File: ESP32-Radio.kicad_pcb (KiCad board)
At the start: 2 copper layers, 69 parts, among them J1 BNC, J11 Conn_01x04_Female, J2 Audio_Jack, J3 Pad, J4 Pad, J6 Audio_Jack, J8 PCB_SMA, T1 6:31, T2 31:6, T3 T50_SPLITTER, T4 T50_SPLITTER, U1 LM358, U10 si5351, U11 LD33V, U2 LM358, U3 LM358, U6 MCP1703A-2502_SOT223, U7 FST3253, U8 FST3253

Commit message: added pa
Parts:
- removed C10, C7, C9: 470nF, Xenir:Capacitor 0805
- removed C15: .1uF, Xenir:Capacitor 0805
- removed C17, C18, C19, C20: 10uF, Xenir:Cap_4x5.4
- removed C28: .1uF, Xenir:Capacitor 1206
- removed J3, J4: Pad, Xenir:Pad
- removed J8: PCB_SMA, Xenir:PCB SMA
- removed R10, R23, R7, R8, R9: 100, Xenir:Resistor 0805
- removed T2: 31:6, Xenir:T37 Transformer
- removed T3, T4: T50_SPLITTER, Xenir:T50 Trifilar
- removed U3: LM358, Xenir:SOIC8
- removed U7: FST3253, Xenir:SO16
- removed VC1, VC2: 40pF, Xenir:trimcap
- added  : MountingHole_3.2mm_M3, MountingHole:MountingHole_3.2mm_M3, F.Cu at (262.4, 96.0)
- added  : MountingHole_3.2mm_M3, MountingHole:MountingHole_3.2mm_M3, F.Cu at (149.8, 96.0)
- added  : MountingHole_3.2mm_M3, MountingHole:MountingHole_3.2mm_M3, F.Cu at (262.4, 160.4)
- added  : MountingHole_3.2mm_M3, MountingHole:MountingHole_3.2mm_M3, F.Cu at (149.8, 160.4)
- added C51: .1uF, Xenir:Capacitor 0805, F.Cu at (206.2, 118.8)
- added C52: .1uF, Xenir:Capacitor 0805, F.Cu at (208.0, 120.6)
- added C53: .1uF, Xenir:Capacitor 0805, F.Cu at (200.7, 96.9)
- added C55: .1uF, Xenir:Capacitor 0805, F.Cu at (222.0, 127.1)
- added C57: .1uF, Xenir:Capacitor 0805, F.Cu at (239.1, 140.0)
- added D1: 1N914, Diode_SMD:D_SOD-323_HandSoldering, F.Cu at (222.5, 122.2)
- added D2: D_Zener, Diode_THT:D_A-405_P10.16mm_Horizontal, F.Cu at (230.2, 142.5)
- added L1: Inductor, Xenir:T37_Inductor, F.Cu at (214.2, 104.9)
- added L2: Inductor, Xenir:T37_Inductor, F.Cu at (234.7, 98.9)
- added L3: 10T T37-6, Xenir:T37_Inductor, F.Cu at (253.7, 133.4)
- added L4: 11T T37-6, Xenir:T37_Inductor, F.Cu at (239.9, 121.7)
- added Q1: 2N3904-SMD, Package_TO_SOT_SMD:SOT-23, F.Cu at (206.5, 125.5)
- added Q2: 2SC5706, Package_TO_SOT_SMD:TO-252-2, F.Cu at (213.1, 115.0)
- added Q3: 2SC5706, Package_TO_SOT_SMD:TO-252-2, F.Cu at (230.0, 119.5)
- added R52: 1k, Xenir:Resistor 0805, F.Cu at (221.5, 122.1)
- added R53: 1k, Xenir:Resistor 0805, F.Cu at (215.9, 128.5)
- added R54: 10k, Xenir:Resistor 0805, F.Cu at (214.4, 118.7)
- added R55: 10, Xenir:Resistor 0805, F.Cu at (217.0, 112.2)
- added R56: 1k, Xenir:Resistor 0805, F.Cu at (205.8, 111.2)
- added R57: 1k, Xenir:Resistor 0805, F.Cu at (220.0, 127.1)
- added R58: 100, Xenir:Resistor 0805, F.Cu at (226.6, 125.2)
- added R59: 1, Resistor_THT:R_Axial_DIN0204_L3.6mm_D1.6mm_P2.54mm_Vertical, F.Cu at (230.2, 133.2)
- added R60: 1, Resistor_THT:R_Axial_DIN0204_L3.6mm_D1.6mm_P2.54mm_Vertical, F.Cu at (230.2, 137.2)
- C1, C2: value 1nF -> .1uF
- C3: value 150pF -> 220pF
- C4: value 5pF -> 150pF
- C5: value 10pF -> 470pF
- C6: value 150pF -> .1uF; footprint Xenir:Capacitor 1206 -> Xenir:Capacitor 0805
- C8: value 470nF -> 330pF; footprint Xenir:Capacitor 0805 -> Xenir:Capacitor 1206
- J1: value BNC -> Jack-DC; footprint Xenir:BNC -> Connector_BarrelJack:BarrelJack_Horizontal; moved to B.Cu
- J11, J6, U10, U11: moved to B.Cu
- J2: value Audio_Jack -> BNC; footprint Xenir:Audio_Jack -> Xenir:BNC; moved to B.Cu
- R5: value 10k -> 1k
- R6: value 10k -> 100
- T1: value 6:31 -> T37_XFRM
- moved T1 114.7 mm to (215.3, 133.6), turned to 270 degrees
- moved J2 106.0 mm to (246.5, 100.2), turned to 180 degrees
- moved U10 97.9 mm to (196.0, 133.2), turned to 180 degrees
- moved C3 94.4 mm to (239.1, 141.0), turned to 180 degrees
- moved C5 85.1 mm to (249.8, 131.2), turned to 180 degrees
- moved U8 80.8 mm to (203.1, 148.9), turned to 90 degrees
- moved R6 71.7 mm to (211.6, 123.5)
- moved C8 71.6 mm to (249.8, 114.0)
- moved C6 70.7 mm to (218.2, 97.8), turned to 180 degrees
- moved U2 69.2 mm to (184.3, 153.1), turned to 270 degrees
- moved C30 66.7 mm to (209.0, 158.0), turned to 180 degrees
- moved C21 63.3 mm to (163.6, 105.0)
- moved J1 63.3 mm to (156.5, 115.8)
- moved C4 62.8 mm to (221.3, 112.7)
- moved C11 61.6 mm to (186.3, 100.3), turned to 270 degrees
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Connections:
- C1 pad 1: I_OUTPUT -> Net-(C1-Pad1)
- C1 pad 2: Net-(C1-Pad2) -> Q_Out
- C2 pad 1: Q_OUTPUT -> Net-(C2-Pad1)
- C2 pad 2: Net-(C2-Pad2) -> I_Out
- C3 pad 1: GND -> Net-(C3-Pad1)
- C3 pad 2: Net-(C3-Pad2) -> GND
- C4 pad 1: Net-(C3-Pad2) -> Net-(C4-Pad1)
- C5 pad 1: Net-(C3-Pad2) -> Net-(C5-Pad1)
- C5 pad 2: Net-(C4-Pad2) -> GND
- C6 pad 1: GND -> +12V
- C6 pad 2: Net-(C4-Pad2) -> GND
- C8 pad 1: GND -> Net-(C8-Pad1)
- C8 pad 2: Net-(C8-Pad2) -> GND
- J6 pad RING: AudioIn -> I_Out
- J6 pad RSH: AudioIn -> I_Out
- J6 pad TIP: AudioIn -> Q_Out
- J6 pad TSH: AudioIn -> Q_Out
- R1 pad 1: (no net) -> Net-(C1-Pad1)
- R11 pad 1: Net-(C17-Pad1) -> Net-(R11-Pad1)
- R12 pad 1: Net-(C19-Pad1) -> Net-(R12-Pad1)
- R13 pad 2: Net-(C18-Pad1) -> Net-(R13-Pad2)
- R14 pad 2: Net-(C20-Pad1) -> Net-(R14-Pad2)
- R17 pad 1: Net-(C17-Pad2) -> Net-(R11-Pad1)
- R18 pad 1: Net-(C18-Pad2) -> Net-(R13-Pad2)
- R19 pad 1: Net-(C19-Pad2) -> Net-(R12-Pad1)
- R2 pad 1: (no net) -> Net-(C2-Pad1)
- R20 pad 1: Net-(C20-Pad2) -> Net-(R14-Pad2)
- R3 pad 2: Net-(C17-Pad1) -> Net-(R11-Pad1)
- R4 pad 2: Net-(C19-Pad1) -> Net-(R12-Pad1)
- R5 pad 1: Net-(C1-Pad2) -> Net-(R5-Pad1)
- R5 pad 2: I_OUTPUT -> Net-(R5-Pad2)
- R6 pad 1: Net-(C2-Pad2) -> Net-(C51-Pad1)
- R6 pad 2: Q_OUTPUT -> GND
- T1 pad C1A: GND -> Net-(Q1-Pad1)
- T1 pad C1B: Net-(J1-PadS) -> Net-(R5-Pad1)
- T1 pad C2A: GND -> Net-(R5-Pad2)
- T1 pad C2B: Net-(C3-Pad2) -> Net-(Q1-Pad1)
- U1 pad 1: Net-(C17-Pad1) -> Net-(R11-Pad1)
- U1 pad 7: Net-(C18-Pad1) -> Net-(R13-Pad2)
- U10 pad 0: LO_0 -> LO_90
- U10 pad 2: LO_90 -> LO_0
- U2 pad 1: Net-(C19-Pad1) -> Net-(R12-Pad1)
- U2 pad 7: Net-(C20-Pad1) -> Net-(R14-Pad2)
- U8 pad 7: Net-(T4-PadC2B) -> Net-(R5-Pad2)
- U8 pad 9: Net-(T4-PadC3A) -> Net-(R5-Pad1)
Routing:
- net +12V: track 0.00 -> 231.4 mm, vias 0 -> 4
- net +5V: track 0.00 -> 131.2 mm, vias 0 -> 3
- net +2V5: track 0.00 -> 79.2 mm, vias 0 -> 2
- net Net-(C57-Pad1): track 0.00 -> 55.0 mm, vias 0 -> 12
- net GND: track 0.00 -> 51.8 mm, vias 0 -> 3
- net 0: track 0.00 -> 49.7 mm, vias 0 -> 2
- net Net-(R12-Pad1): track 0.00 -> 48.3 mm, vias 0 -> 4
- net 90: track 0.00 -> 43.1 mm, vias 0 -> 2
- net LO_90: track 0.00 -> 42.9 mm, vias 0 -> 2
- net Net-(R11-Pad1): track 0.00 -> 34.3 mm, vias 0 -> 2
- net Net-(J11-Pad2): track 0.00 -> 33.3 mm
- net LO_0: track 0.00 -> 33.1 mm, vias 0 -> 2
- net 270: track 0.00 -> 32.3 mm, vias 0 -> 2
- net Net-(J11-Pad1): track 0.00 -> 30.2 mm
- net Net-(C4-Pad1): track 0.00 -> 28.6 mm
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- added copper zone on B.Cu, net GND
- added copper zone on F.Cu, net GND
- added copper zone on B.Cu, net Net-(C57-Pad1)
- added copper zone on F.Cu, net Net-(C57-Pad1)
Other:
- board outline added: 119.8 x 71.5 mm
- rule pad_to_mask_clearance: 0.051 -> 0
- board text added: "NA5Y Tayloe Mixer"

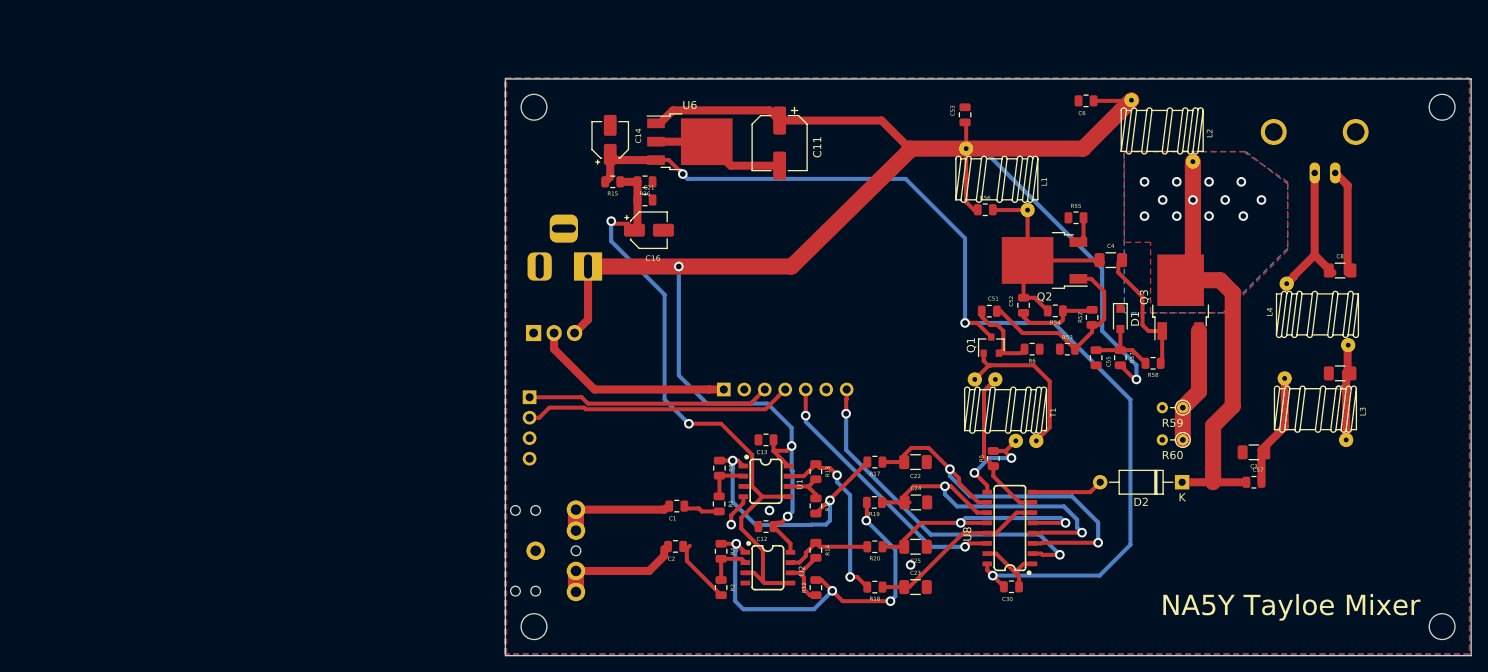
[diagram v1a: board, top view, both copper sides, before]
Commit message: added emiiter smd resistor
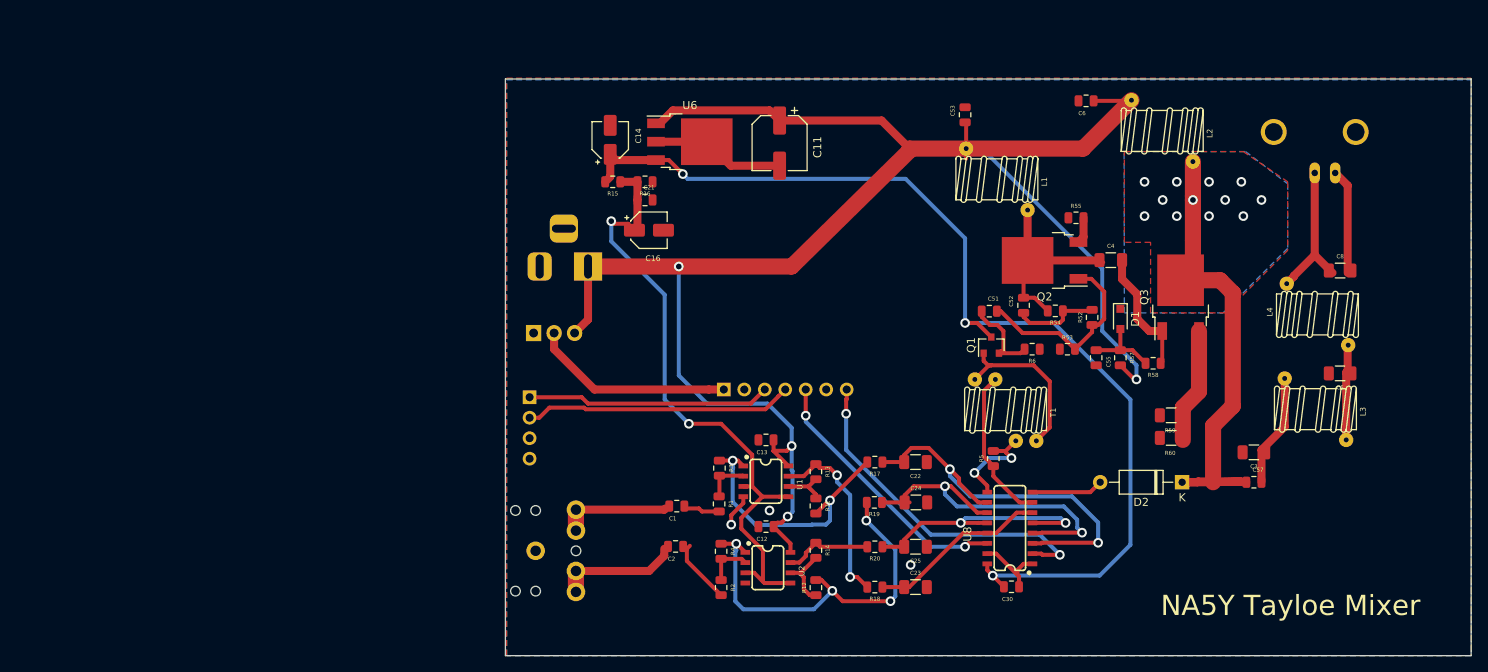
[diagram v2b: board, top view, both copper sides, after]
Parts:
- removed  : MountingHole_3.2mm_M3, MountingHole:MountingHole_3.2mm_M3 (x4)
- removed R56: 1k, Xenir:Resistor 0805
- R59, R60: footprint Resistor_THT:R_Axial_DIN0204_L3.6mm_D1.6mm_P2.54mm_Vertical -> Xenir:Resistor 1206
- moved R59 3.68 mm to (228.7, 136.6)
- moved R60 2.65 mm to (228.7, 139.4)
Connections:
- R59 pad 2: GND -> (no net)
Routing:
- net Net-(C57-Pad1): track 55.0 -> 62.2 mm
- net +12V: track 231.4 -> 224.2 mm
- net Net-(C4-Pad1): track 28.6 -> 33.2 mm
